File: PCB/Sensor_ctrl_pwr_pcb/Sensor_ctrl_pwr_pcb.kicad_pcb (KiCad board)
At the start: 2 copper layers, 28 x 42.6 mm, 17 parts, among them J1 BATTERY 320 mAh, J2 TFT SCREEN PINOUT, Q1 PMOS, U1 AP2112K-3.3, U2 TP4056-42-ESOP8, U3 ESP32C3-SUPERMINI, U4 module_max30102

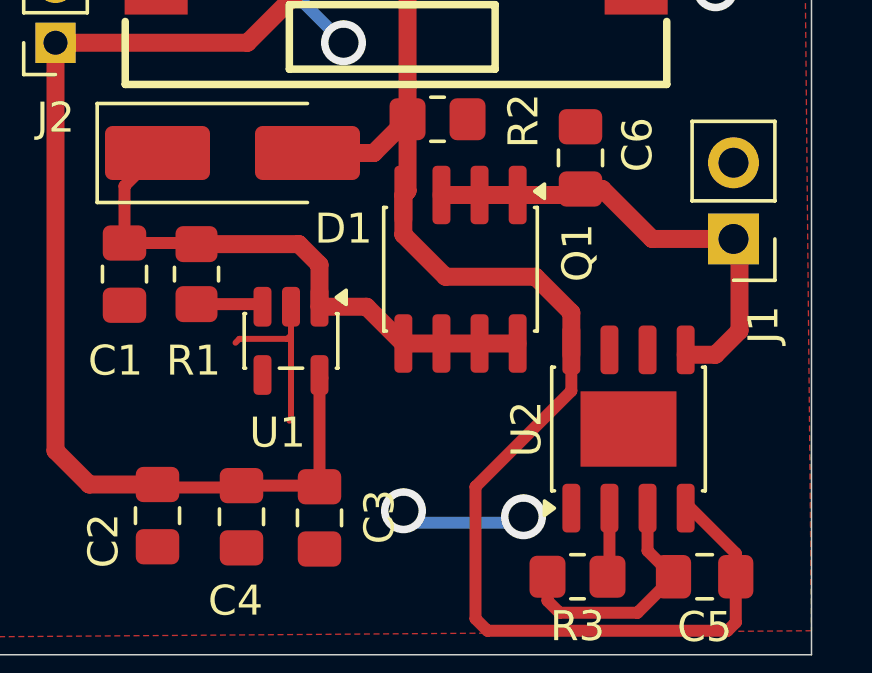
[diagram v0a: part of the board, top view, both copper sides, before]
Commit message: Arreglo de routeo de PCB con respecto al MOSFET PMOS
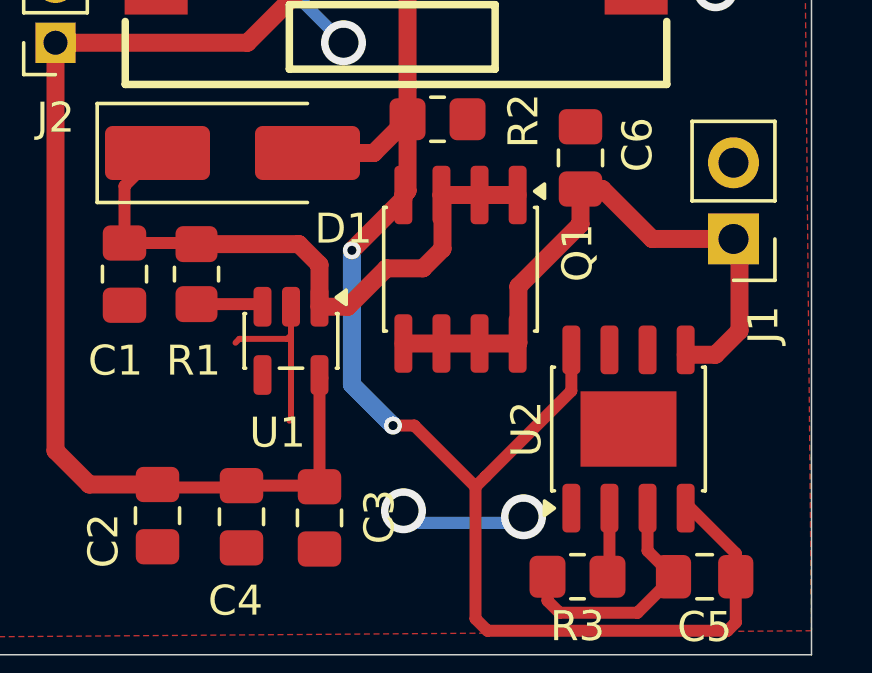
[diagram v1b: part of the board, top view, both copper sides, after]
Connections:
- Q1 pad 1: VBAT -> Net-(D1-K)
- Q1 pad 2: VBAT -> Net-(D1-K)
- Q1 pad 3: VBAT -> Net-(D1-K)
- Q1 pad 5: Net-(D1-K) -> VBAT
- Q1 pad 6: Net-(D1-K) -> VBAT
- Q1 pad 7: Net-(D1-K) -> VBAT
- Q1 pad 8: Net-(D1-K) -> VBAT
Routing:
- net VBAT: track 15.8 -> 21.2 mm
- net VBUS: track 66.6 -> 69.7 mm, vias 0 -> 2
- net Net-(D1-K): track 18.8 -> 20.9 mm
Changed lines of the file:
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@@
 			(layers "F.Cu" "F.Mask" "F.Paste")
 			(roundrect_rratio 0.25)
-			(net 5 "VBAT")
+			(net 2 "Net-(D1-K)")
 			(pinfunction "D")
 			(pintype "passive")
@@
 			(layers "F.Cu" "F.Mask" "F.Paste")
 			(roundrect_rratio 0.25)
-			(net 5 "VBAT")
+			(net 2 "Net-(D1-K)")
 			(pinfunction "G")
 			(pintype "input")
@@
 			(layers "F.Cu" "F.Mask" "F.Paste")
 			(roundrect_rratio 0.25)
-			(net 5 "VBAT")
+			(net 2 "Net-(D1-K)")
 			(pinfunction "S")
 			(pintype "passive")
@@
 			(layers "F.Cu" "F.Mask" "F.Paste")
 			(roundrect_rratio 0.25)
-			(net 2 "Net-(D1-K)")
+			(net 5 "VBAT")
 		)
 		(pad "6" smd roundrect
@@
 			(layers "F.Cu" "F.Mask" "F.Paste")
 			(roundrect_rratio 0.25)
-			(net 2 "Net-(D1-K)")
+			(net 5 "VBAT")
 		)
 		(pad "7" smd roundrect
@@
 			(layers "F.Cu" "F.Mask" "F.Paste")
 			(roundrect_rratio 0.25)
-			(net 2 "Net-(D1-K)")
+			(net 5 "VBAT")
 		)
 		(pad "8" smd roundrect
@@
 			(layers "F.Cu" "F.Mask" "F.Paste")
 			(roundrect_rratio 0.25)
-			(net 2 "Net-(D1-K)")
+			(net 5 "VBAT")
 		)
 		(embedded_fonts no)
@@
 	)
 	(segment
-		(start 151.865 113.225)
-		(end 154.405 113.225)
-		(width 0.6)
+		(start 141.3 109.875)
+		(end 143.6625 109.875)
+		(width 0.4)
 		(layer "F.Cu")
 		(net 2)
 	)
 	(segment
-		(start 141.3 109.875)
-		(end 143.6625 109.875)
-		(width 0.4)
+		(start 150.03 110.72)
+		(end 151.25 110.72)
+		(width 0.6)
 		(layer "F.Cu")
 		(net 2)
@@
 	)
 	(segment
-		(start 147.8 112)
-		(end 149.37 112)
+		(start 151.9 108.31)
+		(end 151.865 108.275)
 		(width 0.6)
 		(layer "F.Cu")
@@
 	)
 	(segment
-		(start 150.595 113.225)
-		(end 151.865 113.225)
+		(start 148.75 112)
+		(end 150.03 110.72)
 		(width 0.6)
 		(layer "F.Cu")
@@
 	)
 	(segment
-		(start 149.37 112)
-		(end 150.595 113.225)
+		(start 151.25 110.72)
+		(end 151.9 110.07)
+		(width 0.6)
+		(layer "F.Cu")
+		(net 2)
+	)
+	(segment
+		(start 153.135 108.275)
+		(end 154.405 108.275)
+		(width 0.6)
+		(layer "F.Cu")
+		(net 2)
+	)
+	(segment
+		(start 151.865 108.275)
+		(end 153.135 108.275)
+		(width 0.6)
+		(layer "F.Cu")
+		(net 2)
+	)
+	(segment
+		(start 151.9 110.07)
+		(end 151.9 108.31)
 		(width 0.6)
 		(layer "F.Cu")
@@
 	)
 	(segment
+		(start 147.8 112)
+		(end 148.75 112)
+		(width 0.6)
+		(layer "F.Cu")
+		(net 2)
+	)
+	(segment
 		(start 142.4 106.875)
 		(end 141.3 107.975)
@@
 	)
 	(segment
+		(start 150.25 115.96)
+		(end 150.96 115.96)
+		(width 0.4)
+		(layer "F.Cu")
+		(net 4)
+	)
+	(segment
 		(start 153 118)
-		(end 156.195 114.805)
+		(end 153.34 117.66)
 		(width 0.4)
 		(layer "F.Cu")
@@
 	)
 	(segment
-		(start 161.675 120.22)
-		(end 161.675 121)
+		(start 150.96 115.96)
+		(end 153 118)
 		(width 0.4)
 		(layer "F.Cu")
@@
 	)
 	(segment
-		(start 156.195 112.195)
-		(end 156.195 113.6)
-		(width 0.6)
+		(start 161.675 120.22)
+		(end 161.675 121)
+		(width 0.4)
 		(layer "F.Cu")
 		(net 4)
@@
 	)
 	(segment
-		(start 155 111)
-		(end 156.195 112.195)
-		(width 0.6)
-		(layer "F.Cu")
-		(net 4)
-	)
-	(segment
 		(start 150.735 88.265)
 		(end 150.735 105.75)
@@
 	)
 	(segment
-		(start 150.595 108.275)
-		(end 150.595 109.595)
-		(width 0.6)
-		(layer "F.Cu")
-		(net 4)
-	)
-	(segment
 		(start 155 84)
 		(end 150.735 88.265)
@@
 	)
 	(segment
-		(start 150.595 109.595)
-		(end 152 111)
-		(width 0.6)
+		(start 153.34 117.66)
+		(end 156.195 114.805)
+		(width 0.4)
 		(layer "F.Cu")
 		(net 4)
@@
 	)
 	(segment
+		(start 150.595 108.405)
+		(end 148.88 110.12)
+		(width 0.6)
+		(layer "F.Cu")
+		(net 4)
+	)
+	(segment
 		(start 147.4 106.875)
 		(end 149.61 106.875)
@@
 	)
 	(segment
-		(start 152 111)
-		(end 155 111)
+		(start 150.595 108.275)
+		(end 150.595 108.405)
 		(width 0.6)
 		(layer "F.Cu")
 		(net 4)
 	)
+	(via
+		(at 148.88 110.12)
+		(size 0.6)
+		(drill 0.3)
+		(layers "F.Cu" "B.Cu")
+		(net 4)
+	)
+	(via
+		(at 150.25 115.96)
+		(size 0.6)
+		(drill 0.3)
+		(layers "F.Cu" "B.Cu")
+		(net 4)
+	)
+	(segment
+		(start 148.88 114.59)
+		(end 150.25 115.96)
+		(width 0.6)
+		(layer "B.Cu")
+		(net 4)
+	)
+	(segment
+		(start 148.88 110.12)
+		(end 148.88 114.59)
+		(width 0.6)
+		(layer "B.Cu")
+		(net 4)
+	)
+	(segment
+		(start 151.865 113.225)
+		(end 150.595 113.225)
+		(width 0.6)
+		(layer "F.Cu")
+		(net 5)
+	)
+	(segment
+		(start 154.43 113.2)
+		(end 154.405 113.225)
+		(width 0.6)
+		(layer "F.Cu")
+		(net 5)
+	)
 	(segment
 		(start 161.8 112.8)
@@
 	)
 	(segment
-		(start 151.865 108.275)
-		(end 154.405 108.275)
+		(start 154.43 111.32)
+		(end 154.43 113.2)
+		(width 0.6)
+		(layer "F.Cu")
+		(net 5)
+	)
+	(segment
+		(start 156.5 108.075)
+		(end 156.5 109.25)
 		(width 0.6)
 		(layer "F.Cu")
@@
 	)
 	(segment
-		(start 154.405 108.275)
-		(end 156.3 108.275)
+		(start 154.405 113.225)
+		(end 153.135 113.225)
 		(width 0.6)
 		(layer "F.Cu")
@@
 	)
 	(segment
+		(start 156.5 109.25)
+		(end 154.43 111.32)
+		(width 0.6)
+		(layer "F.Cu")
+		(net 5)
+	)
+	(segment
 		(start 161.6 109.74)
 		(end 161.8 109.94)
 		(width 0.6)
 		(layer "F.Cu")
+		(net 5)
+	)
+	(segment
+		(start 151.865 113.225)
+		(end 153.135 113.225)
+		(width 0.6)
+		(layer "F.Cu")
